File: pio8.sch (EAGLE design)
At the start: 35 parts, among them IC1 DS2408, X1 MSTBV3, X7 MSTBV5, X8 MSTBV5

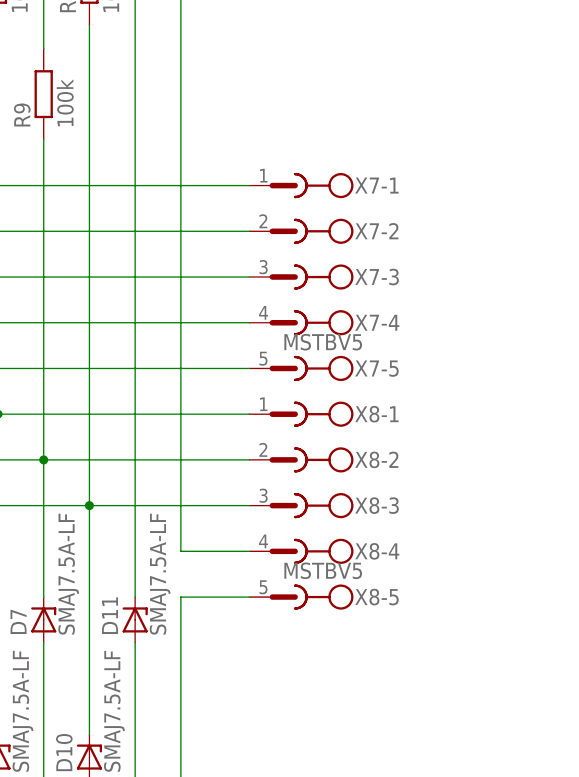
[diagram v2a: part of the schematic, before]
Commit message: changing the connector solution for the digital i/o's - now using spring clamp terminals instead of pluggable screw terminals. The new ones should reduce the width. Also turning back the 3 pin connector so that the screw terminal pints inward
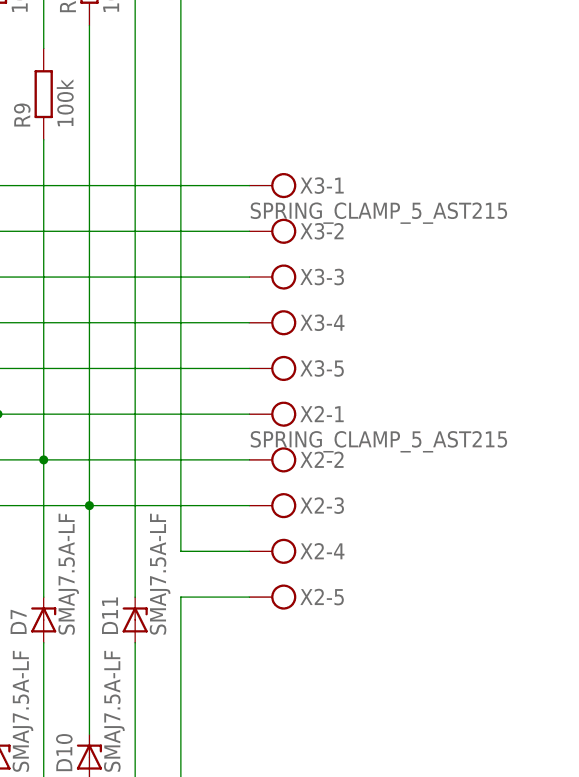
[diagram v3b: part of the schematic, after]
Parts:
- removed X7, X8: MSTBV5, con-phoenix-508:MSTBV5
- added X2, X3: SPRING_CLAMP_5_AST215, connectors:SPRING_CLAMP_5_AST215
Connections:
- net GND: now also X2-5.KL; no longer X8-5.1
- net N$1: now also X3-1.KL; no longer X7-1.1
- net N$11: now also X2-4.KL; no longer X8-4.1
- net N$12: now also X2-3.KL; no longer X8-3.1
- net N$2: now also X3-2.KL; no longer X7-2.1
- net N$3: now also X3-3.KL; no longer X7-3.1
- net N$4: now also X3-4.KL; no longer X7-4.1
- net N$5: now also X3-5.KL; no longer X7-5.1
- net N$6: now also X2-1.KL; no longer X8-1.1
- net N$7: now also X2-2.KL; no longer X8-2.1
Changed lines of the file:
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@@
 <part name="R16" library="rcl" deviceset="R-EU_" device="R0402" value="5.1"/>
 <part name="R18" library="resistor" deviceset="R-EU_" device="R0402" value="100k"/>
-<part name="X7" library="con-phoenix-508" deviceset="MSTBV5" device=""/>
-<part name="X8" library="con-phoenix-508" deviceset="MSTBV5" device=""/>
 <part name="R17" library="resistor" deviceset="R-EU_" device="R0402" value="100k"/>
 <part name="D10" library="diodes" deviceset="ZENER" device="" value="SMAJ7.5A-LF"/>
@@
 <part name="R19" library="rcl" deviceset="R-EU_" device="R0402" value="5.1"/>
 <part name="X1" library="con-phoenix-508" deviceset="MSTBV3" device=""/>
+<part name="X2" library="connectors" deviceset="SPRING_CLAMP_5" device="_AST215"/>
+<part name="X3" library="connectors" deviceset="SPRING_CLAMP_5" device="_AST215"/>
 </parts>
 <sheets>
@@
 <instance part="R16" gate="G$1" x="134.62" y="48.26"/>
 <instance part="R18" gate="G$1" x="124.46" y="88.9" rot="R90"/>
-<instance part="X7" gate="-1" x="213.36" y="78.74" rot="R180"/>
-<instance part="X7" gate="-2" x="213.36" y="73.66" rot="R180"/>
-<instance part="X7" gate="-3" x="213.36" y="68.58" rot="R180"/>
-<instance part="X7" gate="-4" x="213.36" y="63.5" rot="R180"/>
-<instance part="X7" gate="-5" x="213.36" y="58.42" rot="R180"/>
-<instance part="X8" gate="-1" x="213.36" y="53.34" rot="R180"/>
-<instance part="X8" gate="-2" x="213.36" y="48.26" rot="R180"/>
-<instance part="X8" gate="-3" x="213.36" y="43.18" rot="R180"/>
-<instance part="X8" gate="-4" x="213.36" y="38.1" rot="R180"/>
-<instance part="X8" gate="-5" x="213.36" y="33.02" rot="R180"/>
 <instance part="R17" gate="G$1" x="190.5" y="101.6" rot="R90"/>
 <instance part="D10" gate="G$1" x="190.5" y="15.24" rot="R90"/>
@@
 <instance part="X1" gate="-2" x="0" y="71.12"/>
 <instance part="X1" gate="-3" x="0" y="66.04"/>
+<instance part="X2" gate="-1" x="208.28" y="53.34"/>
+<instance part="X2" gate="-2" x="208.28" y="48.26"/>
+<instance part="X2" gate="-3" x="208.28" y="43.18"/>
+<instance part="X2" gate="-4" x="208.28" y="38.1"/>
+<instance part="X2" gate="-5" x="208.28" y="33.02"/>
+<instance part="X3" gate="-1" x="208.28" y="78.74"/>
+<instance part="X3" gate="-2" x="208.28" y="73.66"/>
+<instance part="X3" gate="-3" x="208.28" y="68.58"/>
+<instance part="X3" gate="-4" x="208.28" y="63.5"/>
+<instance part="X3" gate="-5" x="208.28" y="58.42"/>
 </instances>
 <busses>
@@
 <pinref part="R10" gate="G$1" pin="2"/>
 <wire x1="139.7" y1="78.74" x2="154.94" y2="78.74" width="0.1524" layer="91"/>
-<pinref part="X7" gate="-1" pin="1"/>
 <wire x1="154.94" y1="78.74" x2="208.28" y2="78.74" width="0.1524" layer="91"/>
+<pinref part="X3" gate="-1" pin="KL"/>
 </segment>
 </net>
@@
 <pinref part="R11" gate="G$1" pin="2"/>
 <wire x1="147.32" y1="73.66" x2="160.02" y2="73.66" width="0.1524" layer="91"/>
-<pinref part="X7" gate="-2" pin="1"/>
 <wire x1="208.28" y1="73.66" x2="160.02" y2="73.66" width="0.1524" layer="91"/>
+<pinref part="X3" gate="-2" pin="KL"/>
 </segment>
 </net>
@@
 <pinref part="R12" gate="G$1" pin="2"/>
 <wire x1="139.7" y1="68.58" x2="165.1" y2="68.58" width="0.1524" layer="91"/>
-<pinref part="X7" gate="-3" pin="1"/>
 <wire x1="165.1" y1="68.58" x2="208.28" y2="68.58" width="0.1524" layer="91"/>
+<pinref part="X3" gate="-3" pin="KL"/>
 </segment>
 </net>
@@
 <pinref part="R13" gate="G$1" pin="2"/>
 <wire x1="147.32" y1="63.5" x2="170.18" y2="63.5" width="0.1524" layer="91"/>
-<pinref part="X7" gate="-4" pin="1"/>
 <wire x1="208.28" y1="63.5" x2="170.18" y2="63.5" width="0.1524" layer="91"/>
+<pinref part="X3" gate="-4" pin="KL"/>
 </segment>
 </net>
@@
 <pinref part="R14" gate="G$1" pin="2"/>
 <wire x1="139.7" y1="58.42" x2="175.26" y2="58.42" width="0.1524" layer="91"/>
-<pinref part="X7" gate="-5" pin="1"/>
 <wire x1="175.26" y1="58.42" x2="208.28" y2="58.42" width="0.1524" layer="91"/>
+<pinref part="X3" gate="-5" pin="KL"/>
 </segment>
 </net>
@@
 <pinref part="R15" gate="G$1" pin="2"/>
 <wire x1="147.32" y1="53.34" x2="180.34" y2="53.34" width="0.1524" layer="91"/>
-<pinref part="X8" gate="-1" pin="1"/>
 <wire x1="208.28" y1="53.34" x2="180.34" y2="53.34" width="0.1524" layer="91"/>
+<pinref part="X2" gate="-1" pin="KL"/>
 </segment>
 </net>
@@
 <pinref part="R16" gate="G$1" pin="2"/>
 <wire x1="139.7" y1="48.26" x2="185.42" y2="48.26" width="0.1524" layer="91"/>
-<pinref part="X8" gate="-2" pin="1"/>
 <wire x1="185.42" y1="48.26" x2="208.28" y2="48.26" width="0.1524" layer="91"/>
+<pinref part="X2" gate="-2" pin="KL"/>
 </segment>
 </net>
@@
 <wire x1="195.58" y1="27.94" x2="195.58" y2="7.62" width="0.1524" layer="91"/>
 <junction x="195.58" y="7.62"/>
-<pinref part="X8" gate="-5" pin="1"/>
 <wire x1="208.28" y1="33.02" x2="200.66" y2="33.02" width="0.1524" layer="91"/>
+<pinref part="X2" gate="-5" pin="KL"/>
 </segment>
 <segment>
@@
 <junction x="195.58" y="111.76"/>
 <wire x1="200.66" y1="111.76" x2="200.66" y2="38.1" width="0.1524" layer="91"/>
-<pinref part="X8" gate="-4" pin="1"/>
 <wire x1="200.66" y1="38.1" x2="208.28" y2="38.1" width="0.1524" layer="91"/>
+<pinref part="X2" gate="-4" pin="KL"/>
 </segment>
 </net>
@@
 <pinref part="R19" gate="G$1" pin="2"/>
 <wire x1="147.32" y1="43.18" x2="190.5" y2="43.18" width="0.1524" layer="91"/>
-<pinref part="X8" gate="-3" pin="1"/>
 <wire x1="208.28" y1="43.18" x2="190.5" y2="43.18" width="0.1524" layer="91"/>
-</segment>
-</net>
+<pinref part="X2" gate="-3" pin="KL"/>
+</segment>
+</net>

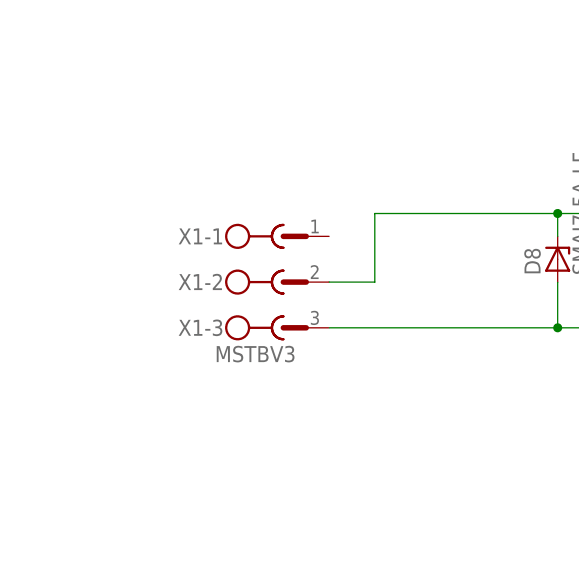
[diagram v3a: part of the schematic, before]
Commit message: changing 1-wire connector to a spring clamp type
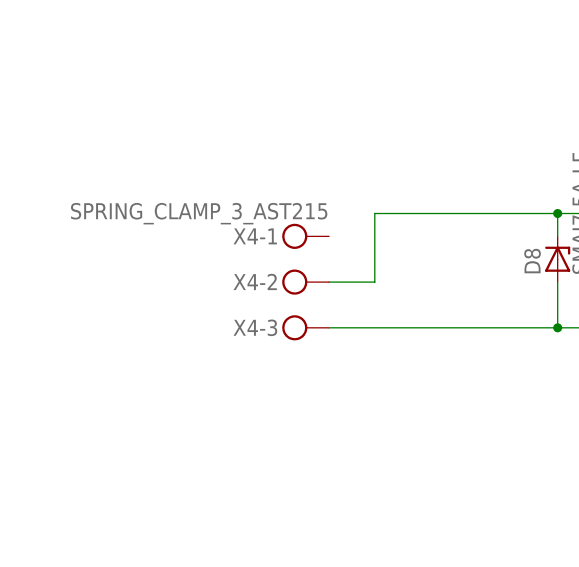
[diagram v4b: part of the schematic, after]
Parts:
- removed X1: MSTBV3, con-phoenix-508:MSTBV3
- added X4: SPRING_CLAMP_3_AST215, connectors:SPRING_CLAMP_3_AST215
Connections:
- net N$10: now also X4-2.KL; no longer X1-2.1
- net N$9: now also X4-3.KL; no longer X1-3.1
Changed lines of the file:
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@@
 <part name="D11" library="diodes" deviceset="ZENER" device="" value="SMAJ7.5A-LF"/>
 <part name="R19" library="rcl" deviceset="R-EU_" device="R0402" value="5.1"/>
-<part name="X1" library="con-phoenix-508" deviceset="MSTBV3" device=""/>
 <part name="X2" library="connectors" deviceset="SPRING_CLAMP_5" device="_AST215"/>
 <part name="X3" library="connectors" deviceset="SPRING_CLAMP_5" device="_AST215"/>
+<part name="X4" library="connectors" deviceset="SPRING_CLAMP_3" device="_AST215"/>
 </parts>
 <sheets>
@@
 <instance part="D11" gate="G$1" x="195.58" y="30.48" rot="R90"/>
 <instance part="R19" gate="G$1" x="142.24" y="43.18"/>
-<instance part="X1" gate="-1" x="0" y="76.2"/>
-<instance part="X1" gate="-2" x="0" y="71.12"/>
-<instance part="X1" gate="-3" x="0" y="66.04"/>
 <instance part="X2" gate="-1" x="208.28" y="53.34"/>
 <instance part="X2" gate="-2" x="208.28" y="48.26"/>
@@
 <instance part="X3" gate="-4" x="208.28" y="63.5"/>
 <instance part="X3" gate="-5" x="208.28" y="58.42"/>
+<instance part="X4" gate="-1" x="5.08" y="76.2" rot="R180"/>
+<instance part="X4" gate="-2" x="5.08" y="71.12" rot="R180"/>
+<instance part="X4" gate="-3" x="5.08" y="66.04" rot="R180"/>
 </instances>
 <busses>
@@
 <junction x="30.48" y="66.04"/>
 <pinref part="D8" gate="G$1" pin="A"/>
-<pinref part="X1" gate="-3" pin="1"/>
+<pinref part="X4" gate="-3" pin="KL"/>
 </segment>
 </net>
@@
 <junction x="30.48" y="78.74"/>
 <pinref part="D8" gate="G$1" pin="C"/>
-<pinref part="X1" gate="-2" pin="1"/>
 <wire x1="5.08" y1="71.12" x2="10.16" y2="71.12" width="0.1524" layer="91"/>
 <wire x1="10.16" y1="71.12" x2="10.16" y2="78.74" width="0.1524" layer="91"/>
-</segment>
-</net>
+<pinref part="X4" gate="-2" pin="KL"/>
+</segment>
+</net>
